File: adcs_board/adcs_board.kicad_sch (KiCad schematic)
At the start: 26 parts, among them J3 USB_B_Micro, J4 Conn_01x04_Pin, U1 STM32F103C8T6, U2 AMS1117-3.3, Y1 16 MHz

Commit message: adcs_board: add coil control, update sensors and apply small fixes
- Implemented control logic for magnetic coils
- Adjusted sensor handling and calibration routines
- Applied minor fixes and improvements across modules
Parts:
- removed J3: USB_B_Micro, Connector_USB:USB_Micro-B_Wuerth_629105150521, symbol Connector:USB_B_Micro
- removed R5: 1K5, Resistor_SMD:R_0402_1005Metric, symbol Device:R
- added C14, C4: 1uF, symbol Device:C
- added C15: 0.01uF, symbol Device:C
- added C16, C17, C18, C19, C20, C21: C, symbol Device:C
- added C68: C0402C103K5RECAUTO, Capacitor_SMD:C_0402_1005Metric_Pad0.74x0.62mm_HandSolder, symbol adcs_board:GRM155R60J106ME15D
- added C69: CL05B104KP5NNNC, Capacitor_SMD:C_0402_1005Metric_Pad0.74x0.62mm_HandSolder, symbol adcs_board:885012206071
- added R2, R3, R54, R7: 4,7k, Resistor_SMD:R_0402_1005Metric_Pad0.72x0.64mm_HandSolder, symbol Device:R
- added U3: I3G4250DTR, adcs:LGA-16_4X4X1_STM, symbol adcs:I3G4250DTR
- added U4: BM1422AGMV-ZE2, adcs:MLGA010V020A_ROM, symbol adcs:BM1422AGMV-ZE2
- added U5, U6, U7: DRV8210DSGR, adcs:DSG0008A-IPC_A, symbol adcs:DRV8210DSGR
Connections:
- net +3.3V: now also C10.1, C5.1, C6.1, C8.1, C9.1, U1.1 (VBAT); no longer C2.1, D1.2 (A), U2.2 (VO)
- net GND: now also C14.2, C15.1, C16.2, C17.2, C18.2, C19.2, C20.2, C21.2, C4.2, C68.2, C69.2, R2.1, R3.1, U3.10 (RES), U3.11 (RES), U3.12 (RES), U3.13 (GND), U3.8 (RES), U3.9 (RES), U4.2 (GND), U4.9 (ADDR), U5.4 (GND), U5.7 (MODE), U5.9 (Thermal_Pad), U6.4 (GND), U6.7 (MODE), U6.9 (Thermal_Pad), U7.4 (GND), U7.7 (MODE), U7.9 (Thermal_Pad)
- net SWCLK: now also U1.37 (PA14); no longer U1.27 (PB14)
- net SWDIO: now also U1.34 (PA13); no longer U1.26 (PB13)
- net MOTORZ1: now reaches U1.12 (PA2)
- net MOTORZ1: now also U6.2 (OUT1)
- net MOTORZ2: now reaches U1.13 (PA3)
- net MOTORZ2: now also U6.3 (OUT2)
- net MOTORY1: now reaches U1.14 (PA4)
- net MOTORY1: now also U7.2 (OUT1)
- net MOTORY2: now reaches U1.15 (PA5)
- net MOTORY2: now also U7.3 (OUT2)
- net MOTORX1: now reaches U1.16 (PA6)
- net MOTORX1: now also U5.2 (OUT1)
- net MOTORX2: now reaches U1.17 (PA7)
- net MOTORX2: now also U5.3 (OUT2)
- net GYRO_I2C_SDL: now reaches U1.21 (PB10)
- net GYRO_I2C_SDL: now also R54.1, U3.2 (SCL/SPC)
- net GYRO_DRDY: now reaches U1.28 (PB15)
- net GYRO_DRDY: now also U3.6 (DRDY/INT2)
- net GYRO_INT: now reaches U1.29 (PA8)
- net GYRO_INT: now also U3.7 (INT1)
- net SCL_MAG: now reaches U1.42 (PB6)
- net SCL_MAG: now also R3.2, U4.7 (SCL)
- net SDA_MAG: now reaches U1.43 (PB7)
- net SDA_MAG: now also R2.2, U4.5 (SDA)
- net USB_D+ renamed GYRO_I2C_SMBAI
- net GYRO_I2C_SMBAI: now also U3.4 (SDO/SA0)
- net USB_D- renamed GYRO_I2C_SDA
- net GYRO_I2C_SDA: now also R7.1, U3.3 (SDA/SDI/SDO)
- new net: C14.1, U4.3 (VREG)
- new net +3.3VA: C4.1, U4.1 (AVDD)
- new net +3V3: C15.2, C16.1, C17.1, C18.1, C19.1, C2.1, C20.1, C21.1, C68.1, C69.1, D1.2 (A), R54.2, R7.2, U2.2 (VO), U3.1 (VDD_IO), U3.15 (RES), U3.16 (VDD), U4.10 (DVDD), U5.1 (VM), U5.8 (VCC), U6.1 (VM), U6.8 (VCC), U7.1 (VM), U7.8 (VCC)
- new net GYRO_I2C_CS: U3.5 (CS)
- new net PLLFILT: U3.14 (PLLFILT)
- new net PWM1: U5.6 (IN1_PH), U6.6 (IN1_PH), U7.6 (IN1_PH)
- new net PWM2: U5.5 (IN2_EN), U6.5 (IN2_EN), U7.5 (IN2_EN)
- no-connect marks 33 -> 22
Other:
- note added: "Coil control X"
- note added: "Coil control Y"
- note added: "Coil control Z"
- note added: "Gyroscope"
- note added: "Magnetometer"
- note removed: "USB App Note AN4875"
- moved on the sheet: C1, C10, C11, C12, C13, C2, C3, C5, C6, C7, C8, C9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

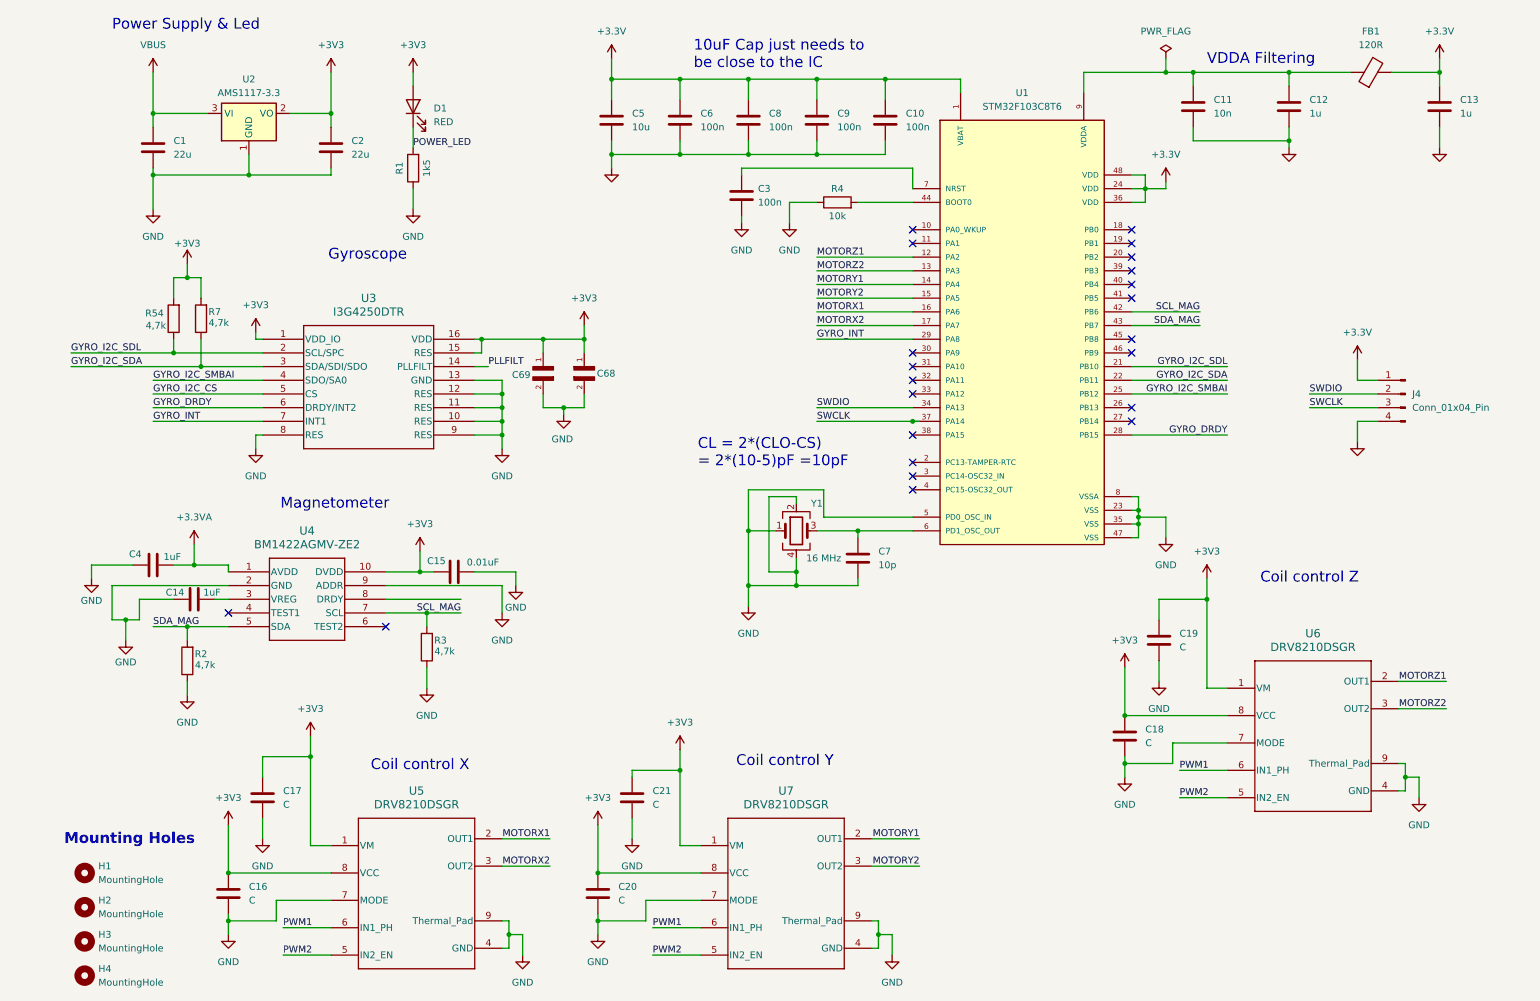
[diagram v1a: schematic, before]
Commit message: adcs_board: schematic corrections and coil control updates
- Fixed schematic errors in ADCS BDOT design
- Updated coil control logic for improved stability
- Minor adjustments to sensor handling and signal routing
- General small fixes and cleanup
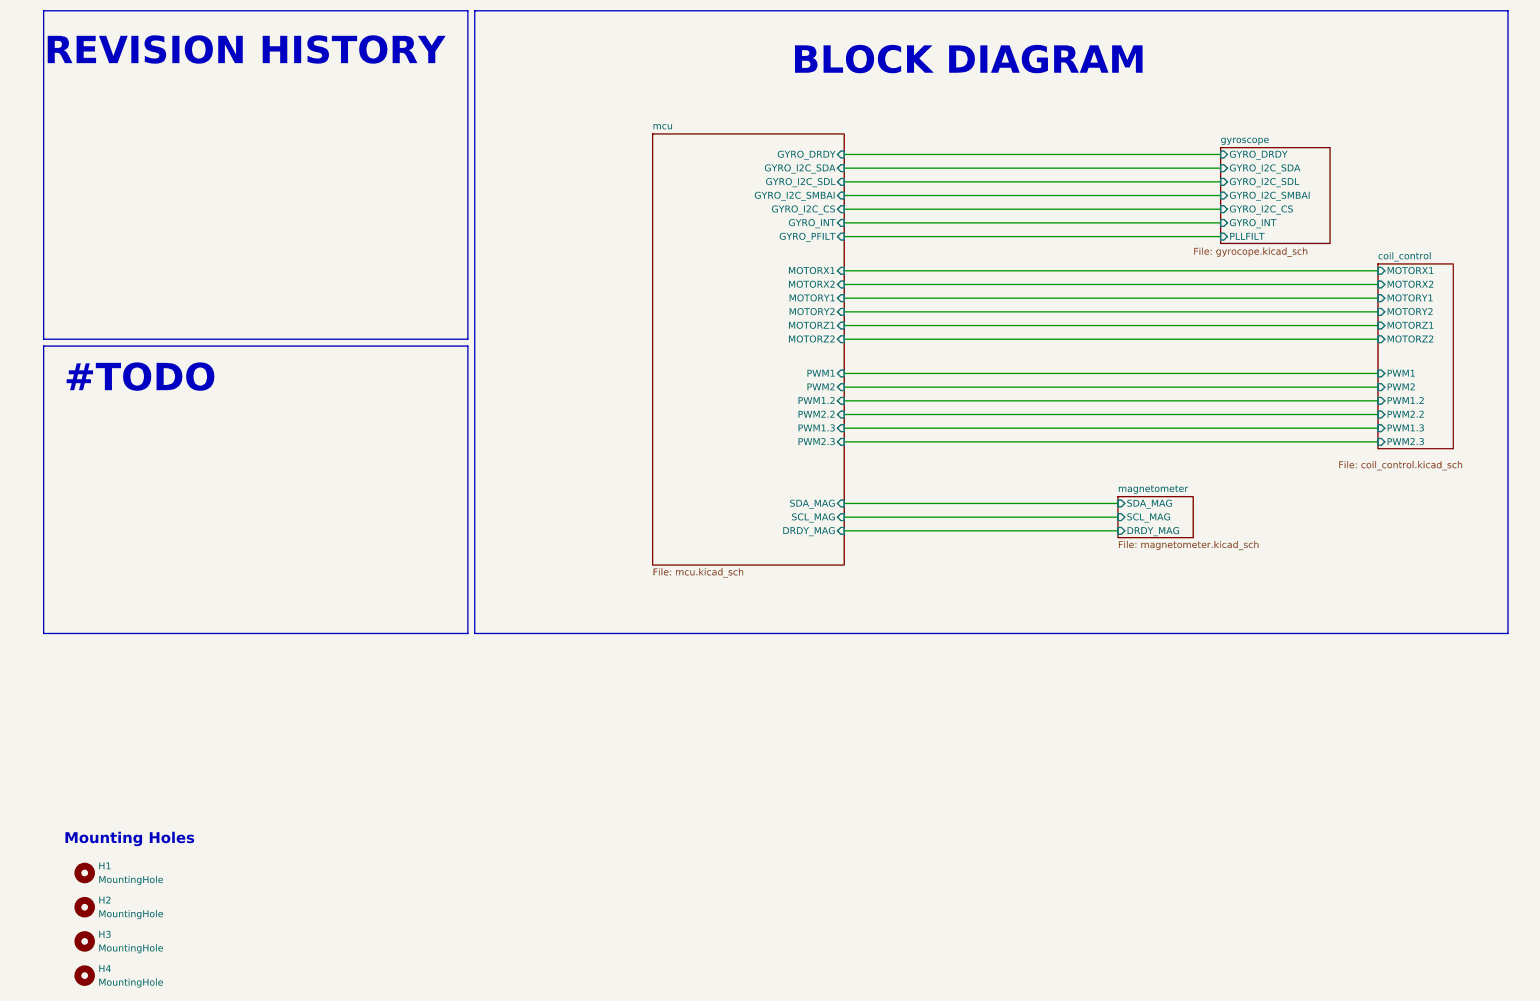
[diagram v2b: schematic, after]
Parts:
- removed C1, C2: 22u, Capacitor_SMD:C_0805_2012Metric, symbol Device:C
- removed C10, C3, C6, C8, C9: 100n, Capacitor_SMD:C_0402_1005Metric, symbol Device:C
- removed C11: 10n, Capacitor_SMD:C_0402_1005Metric, symbol Device:C
- removed C12, C13: 1u, Capacitor_SMD:C_0402_1005Metric, symbol Device:C
- removed C14, C4: 1uF, symbol Device:C
- removed C15: 0.01uF, symbol Device:C
- removed C16, C17, C18, C19, C20, C21: C, symbol Device:C
- removed C5: 10u, Capacitor_SMD:C_0603_1608Metric, symbol Device:C
- removed C68: C0402C103K5RECAUTO, Capacitor_SMD:C_0402_1005Metric_Pad0.74x0.62mm_HandSolder, symbol adcs_board:GRM155R60J106ME15D
- removed C69: CL05B104KP5NNNC, Capacitor_SMD:C_0402_1005Metric_Pad0.74x0.62mm_HandSolder, symbol adcs_board:885012206071
- removed C7: 10p, Capacitor_SMD:C_0402_1005Metric, symbol Device:C
- removed D1: RED, LED_SMD:LED_0603_1608Metric, symbol Device:LED
- removed FB1: 120R, Inductor_SMD:L_0603_1608Metric, symbol Device:FerriteBead
- removed J4: Conn_01x04_Pin, Connector_PinHeader_2.54mm:PinHeader_1x04_P2.54mm_Vertical, symbol Connector:Conn_01x04_Pin
- removed R1: 1k5, Resistor_SMD:R_0402_1005Metric, symbol Device:R
- removed R2, R3, R54, R7: 4,7k, Resistor_SMD:R_0402_1005Metric_Pad0.72x0.64mm_HandSolder, symbol Device:R
- removed R4: 10k, Resistor_SMD:R_0402_1005Metric, symbol Device:R
- removed U1: STM32F103C8T6, adcs:QFP50P900X900X160-48N, symbol adcs:STM32F103C8T6
- removed U2: AMS1117-3.3, Package_TO_SOT_SMD:SOT-223-3_TabPin2, symbol Regulator_Linear:AMS1117-3.3
- removed U3: I3G4250DTR, adcs:LGA-16_4X4X1_STM, symbol adcs:I3G4250DTR
- removed U4: BM1422AGMV-ZE2, adcs:MLGA010V020A_ROM, symbol adcs:BM1422AGMV-ZE2
- removed U5, U6, U7: DRV8210DSGR, adcs:DSG0008A-IPC_A, symbol adcs:DRV8210DSGR
- removed Y1: 16 MHz, Crystal:Crystal_SMD_3225-4Pin_3.2x2.5mm, symbol Device:Crystal_GND24
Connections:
- no-connect marks 22 -> 0
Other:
- added sheet coil_control (coil_control.kicad_sch)
- added sheet gyroscope (gyrocope.kicad_sch)
- added sheet magnetometer (magnetometer.kicad_sch)
- added sheet mcu (mcu.kicad_sch)
- note added: "#TODO"
- note added: "BLOCK DIAGRAM"
- note added: "REVISION HISTORY"
- note removed: "10uF Cap just needs to be close to the IC"
- note removed: "CL = 2*(CLO-CS) = 2*(10-5)pF =10pF"
- note removed: "Coil control X"
- note removed: "Coil control Y"
- note removed: "Coil control Z"
- note removed: "Gyroscope"
- note removed: "Magnetometer"
- note removed: "Power Supply & Led"
- note removed: "VDDA Filtering"

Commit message: adcs_board: resolve schematic ERC violations
- Corrected electrical rule check (ERC) errors in ADCS BDOT schematic
- Fixed unconnected pins and mismatched power nets
- Adjusted symbol properties for proper ERC compliance
- Ensured clean schematic validation with no remaining ERC issues
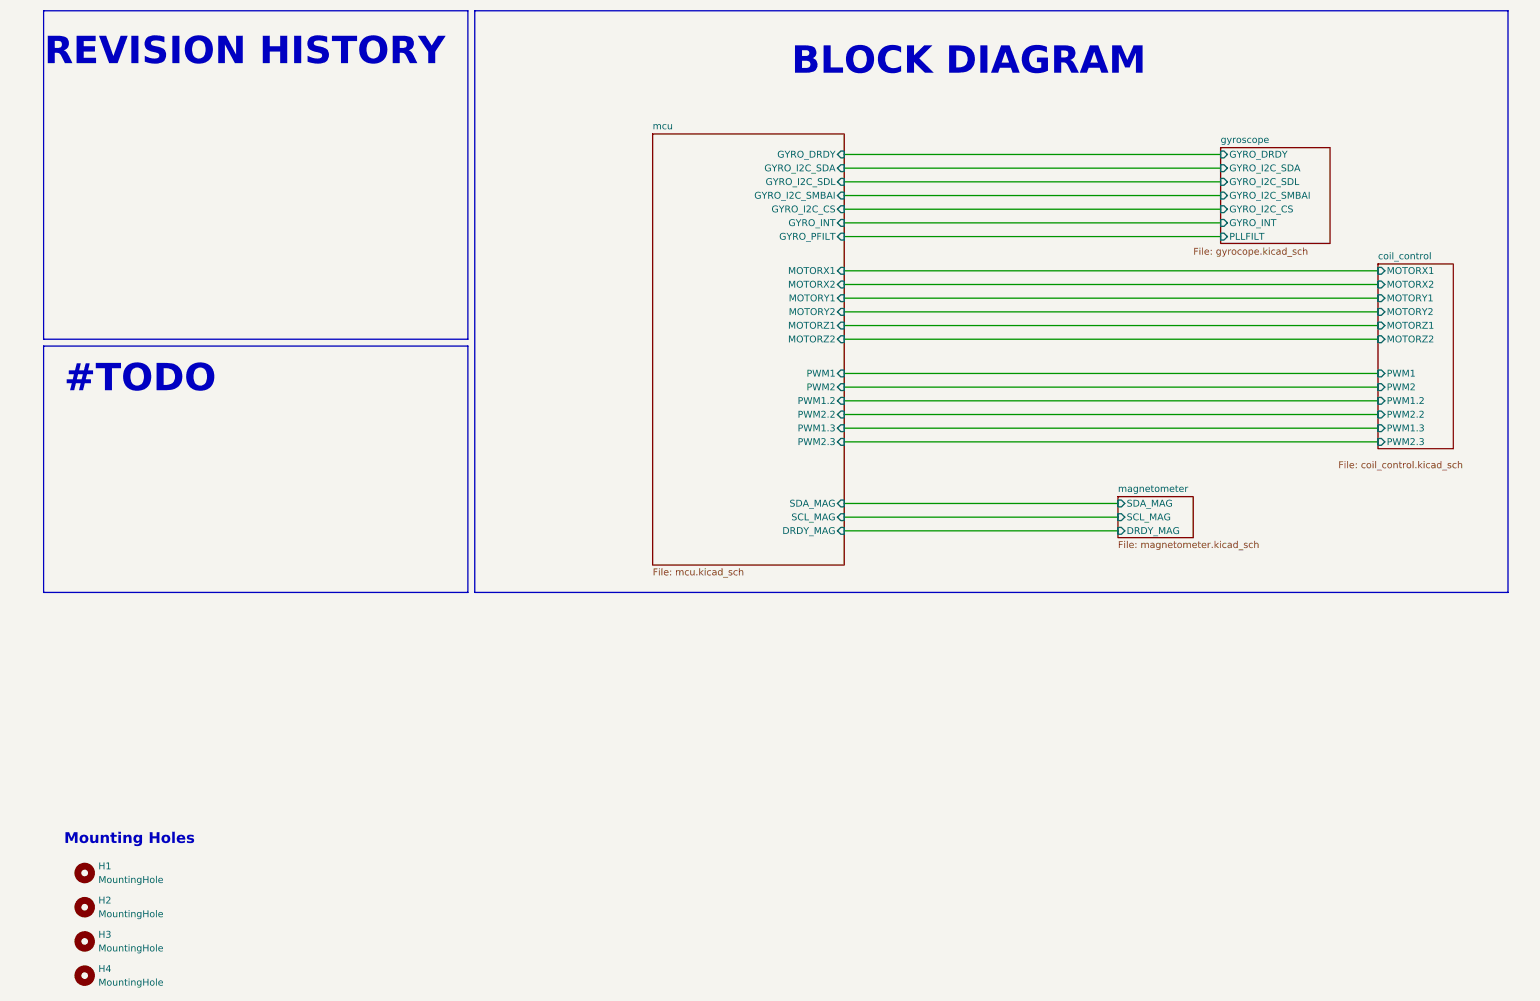
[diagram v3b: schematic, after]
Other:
- title: (none) -> ADCS-BDOT
